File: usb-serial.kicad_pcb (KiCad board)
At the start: 4 copper layers, 68.5 x 42 mm, 42 parts, among them J2 DB25_Plug, U1 ACPL-M50L, U10 TDR2-1222WI, U11 PEME2-5-D12-D, U2 ACPL-M50L, U3 USBLC6-2SC6, U4 ACPL-M50L, U5 ACPL-M50L, U6 Interface_USB_CP2102N-A01-GQF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, U7 SN75155, U8 SN75155, U9 LM1117DT-5.0

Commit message: Add fabrication fies
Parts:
- F1: value Polyfuse -> Polyfuse 1,8A; footprint Fuse:Fuse_0805_2012Metric -> Fuse:Fuse_1206_3216Metric
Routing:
- net GND: track 20.1 -> 21.0 mm, vias 18 -> 20

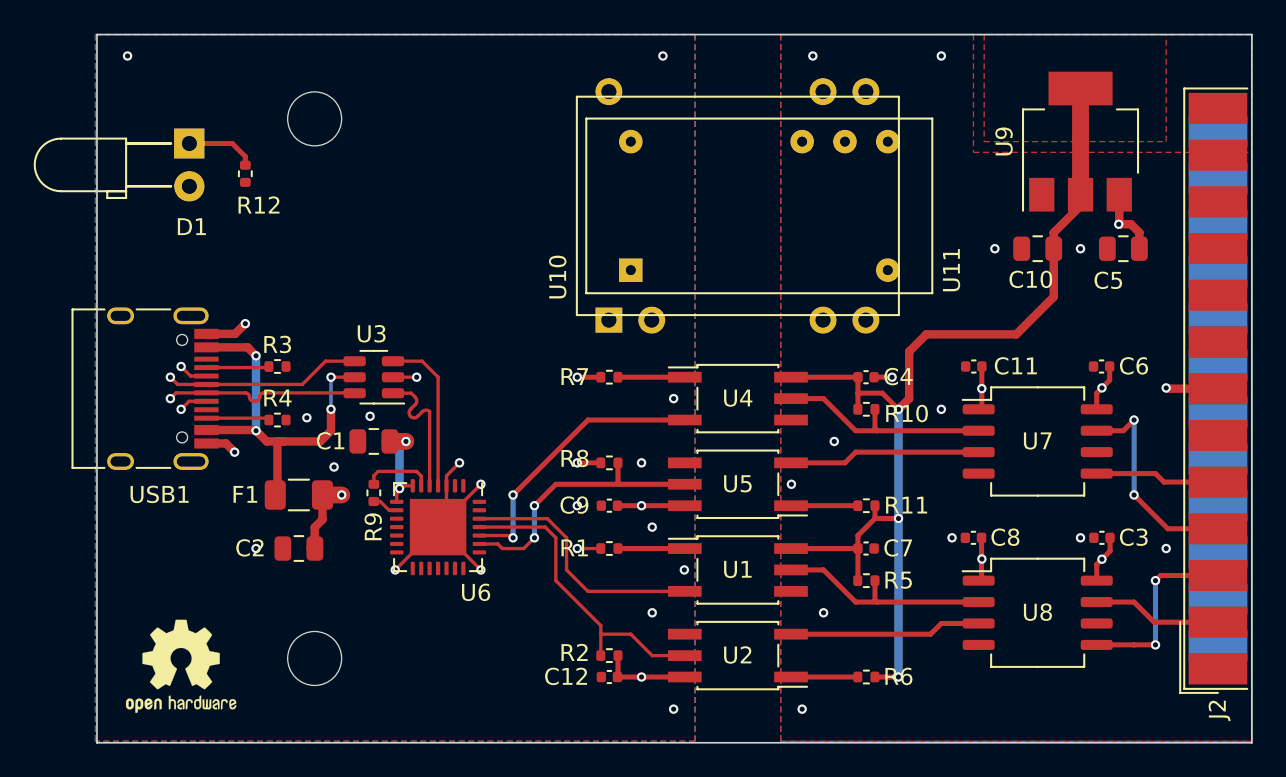
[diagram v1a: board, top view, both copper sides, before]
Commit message: EMC filter according to DC/DC datasheet
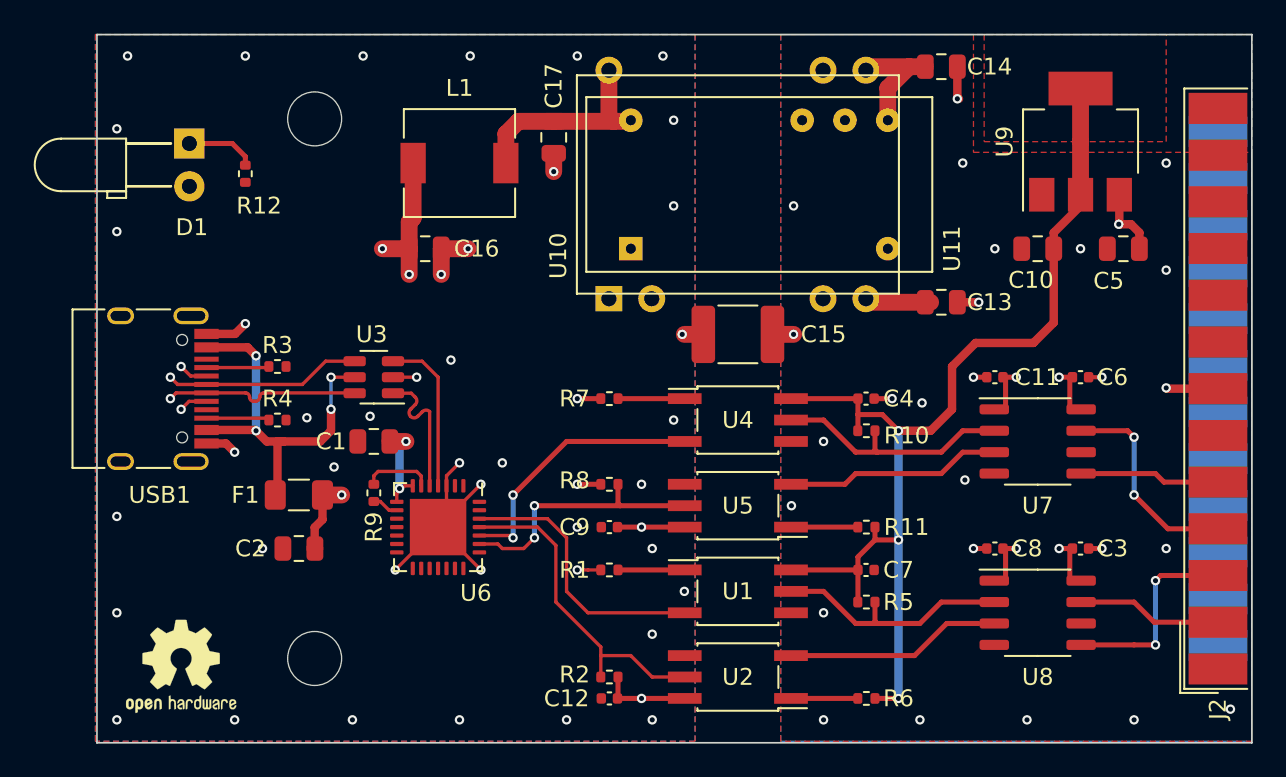
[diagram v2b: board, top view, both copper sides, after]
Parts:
- added C13: 1u, Capacitor_SMD:C_0805_2012Metric, F.Cu at (125.1, 48.9)
- added C14: 1u, Capacitor_SMD:C_0805_2012Metric, F.Cu at (125.1, 34.9)
- added C15: 220pF/3kV Y, Capacitor_SMD:C_1812_4532Metric, F.Cu at (113.0, 50.8)
- added C16: 10u, Capacitor_SMD:C_0805_2012Metric, F.Cu at (94.5, 45.7)
- added C17: 10u, Capacitor_SMD:C_0805_2012Metric, F.Cu at (102.1, 39.1)
- added L1: 2.2uH, Inductor_SMD:L_6.3x6.3_H3, F.Cu at (96.5, 40.6)
- U7, U8: footprint Package_SO:SO-8_5.3x6.2mm_P1.27mm -> Package_SO:SO-8_3.9x4.9mm_P1.27mm
- moved C3 1.42 mm to (133.3, 63.5), turned to 0 degrees
- moved C8 1.42 mm to (128.3, 63.5)
- moved C11 1.40 mm to (128.3, 53.3)
- moved C6 1.40 mm to (133.3, 53.3), turned to 0 degrees
- moved R2 1.27 mm to (105.4, 71.1)
- moved U1 1.27 mm to (113.0, 66.0)
- moved U2 1.27 mm to (113.0, 71.1)
- moved R10 1.27 mm to (120.7, 56.5)
- moved U11 1.27 mm to (106.7, 45.7)
- moved U4 1.27 mm to (113.0, 55.9)
- moved U5 1.27 mm to (113.0, 61.0)
- moved C12 1.27 mm to (105.4, 72.4)
- moved C4 1.27 mm to (120.6, 54.6)
- moved C7 1.27 mm to (120.6, 64.8)
- moved C9 1.27 mm to (105.4, 62.2)
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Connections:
- U10 pad 14: VBUS -> Vfilt
- U11 pad 14: VBUS -> Vfilt
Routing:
- net Vfilt: track 0.00 -> 12.6 mm
- net +12V: track 9.92 -> 18.4 mm
- net VBUS: track 23.6 -> 32.0 mm, vias 8 -> 10
- net GND1: track 4.15 -> 11.5 mm, vias 14 -> 26
- net -12V: track 5.25 -> 10.8 mm
- net GND: track 21.0 -> 26.3 mm, vias 20 -> 41
- net ~{ISO_CTS}: track 11.4 -> 12.8 mm
- net ~{ISO_TXD}: track 13.1 -> 14.6 mm
- net ~{ISO_RTS}: track 13.2 -> 14.7 mm
- net +5V: track 62.9 -> 64.1 mm
- net ~{TXD}: track 15.1 -> 16.4 mm
- net Net-(U7-DY): track 12.7 -> 11.6 mm
- net ~{RXD}: track 18.4 -> 19.4 mm
- net ~{ISO_RXD}: track 11.4 -> 11.9 mm
- net ~{RTS}: track 16.6 -> 16.1 mm
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
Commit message: usb-serial: Change opto to MAX 22246 isolator.
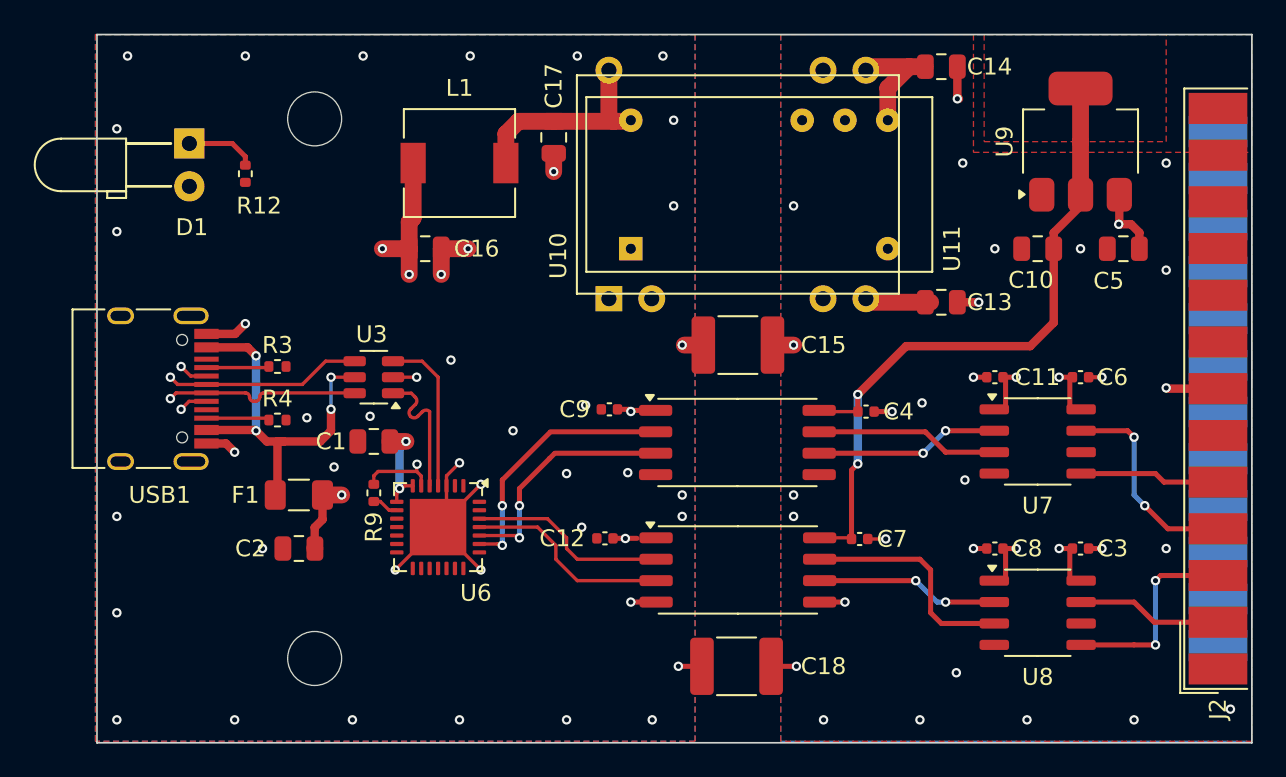
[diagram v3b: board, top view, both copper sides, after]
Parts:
- removed R1, R11, R6, R7: 1k, Resistor_SMD:R_0402_1005Metric
- removed R10, R2, R5, R8: 3k3, Resistor_SMD:R_0402_1005Metric
- removed REF**: OSHW-Logo2_7.3x6mm_SilkScreen, Symbol:OSHW-Logo2_7.3x6mm_SilkScreen
- removed U1, U2, U4, U5: ACPL-M50L, Package_SO:SO-5_4.4x3.6mm_P1.27mm
- added C18: 220pF/3kV Y, Capacitor_SMD:C_1812_4532Metric, F.Cu at (113.0, 70.5)
- added U12: MAX22246, anders:MAX22246, F.Cu at (113.0, 64.8)
- added U13: MAX22246, anders:MAX22246, F.Cu at (113.0, 57.2)
- R12: value 2k2 -> 1k5
- U11: value PEME2-5-D12-D -> <<<<<<s<
- moved C12 9.50 mm to (105.1, 62.9)
- moved C9 6.98 mm to (105.4, 55.2)
- moved C7 1.87 mm to (120.2, 62.9)
- moved C4 0.77 mm to (120.6, 55.4)
- moved C15 0.64 mm to (113.0, 51.4)
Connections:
- C12 pad 1: VBUS -> +3.3V
- C9 pad 1: VBUS -> +3.3V
- R9 pad 2: Net-(U6-VDD) -> +3.3V
- U6 pad 6: Net-(U6-VDD) -> +3.3V
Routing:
- net +3.3V: track 0.00 -> 28.5 mm, vias 0 -> 3
- net +5V: track 64.1 -> 42.3 mm, vias 3 -> 2
- net VBUS: track 32.0 -> 18.5 mm, vias 10 -> 5
- net ~{RXD}: track 19.4 -> 11.9 mm
- net ~{TXD}: track 16.4 -> 11.4 mm
- net Net-(U6-VDD): track 4.12 -> 0.00 mm
- net GND1: track 11.5 -> 15.5 mm, vias 26 -> 29
- net Net-(U5-A1): track 3.96 -> 0.00 mm
- net Net-(U4-A1): track 3.96 -> 0.00 mm
- net Net-(U2-A1): track 3.96 -> 0.00 mm
- net Net-(U1-A1): track 3.96 -> 0.00 mm
- net ~{ISO_RTS}: track 14.7 -> 10.9 mm, vias 0 -> 2
- net ~{ISO_TXD}: track 14.6 -> 11.4 mm, vias 0 -> 2
- net GND: track 26.3 -> 29.2 mm, vias 41 -> 43
- net ~{ISO_RXD}: track 11.9 -> 13.9 mm
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- added copper zone on In2.Cu, net GND
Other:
- board text added: "Isolated USB-RS232 Adapter By Anders Sandahl 2024/2025"
- board text removed: "Isolated USB-RS232 Adapter By Anders Sandahl 2024"

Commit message: Updated 3D image of PCB
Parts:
- U11: value <<<<<<s< -> PEME2-5-D12-D
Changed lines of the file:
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@@
 			)
 		)
-		(property "Value" "<<<<<<s<"
+		(property "Value" "PEME2-5-D12-D"
 			(at 7.43 20.32 90)
 			(layer "F.Fab")
@@
 		(sheetname "Root")
 		(sheetfile "usb-serial.kicad_sch")
-		(attr through_hole exclude_from_pos_files exclude_from_bom)
+		(attr through_hole exclude_from_pos_files)
 		(fp_line
 			(start 8.99 -2.64)
@@
 		)
 		(property "Footprint" "LED_THT:LED_D3.0mm_Horizontal_O3.81mm_Z10.0mm"
-			(at 0 0 -90)
+			(at 0 0 90)
 			(layer "F.Fab")
 			(hide yes)
@@
 		)
 		(property "Datasheet" ""
-			(at 0 0 -90)
+			(at 0 0 90)
 			(layer "F.Fab")
 			(hide yes)
@@
 		)
 		(property "Description" ""
-			(at 0 0 -90)
+			(at 0 0 90)
 			(layer "F.Fab")
 			(hide yes)
@@
 		(sheetname "Root")
 		(sheetfile "usb-serial.kicad_sch")
-		(attr through_hole exclude_from_pos_files exclude_from_bom)
+		(attr through_hole exclude_from_pos_files)
 		(fp_line
 			(start 2.83 4.87)
@@
 		)
 		(fp_text user "${REFERENCE}"
-			(at 1.27 5.66 -90)
+			(at 1.27 5.66 90)
 			(layer "F.Fab")
 			(effects
@@
 		(model "${KICAD8_3DMODEL_DIR}/LED_THT.3dshapes/LED_D3.0mm_Horizontal_O3.81mm_Z10.0mm.wrl"
 			(offset
-				(xyz 0 0 0)
+				(xyz 0 0 -8)
 			)
 			(scale
@@
 		(sheetname "Root")
 		(sheetfile "usb-serial.kicad_sch")
-		(attr exclude_from_pos_files exclude_from_bom)
+		(attr exclude_from_pos_files)
 		(fp_circle
 			(center 0 0)
@@
 		(sheetname "Root")
 		(sheetfile "usb-serial.kicad_sch")
-		(attr smd exclude_from_pos_files exclude_from_bom)
+		(attr smd exclude_from_pos_files)
 		(fp_line
 			(start -18.043333 -2.24)
@@
 			(pintype "passive+no_connect")
 		)
-		(model "${KICAD8_3DMODEL_DIR}/Connector_Dsub.3dshapes/DSUB-25_Male_EdgeMount_P2.77mm.wrl"
+		(model "/home/anders/.local/share/kicad/8.0/3dmodels/dsub-db25-male-171-025-103.STEP"
 			(offset
-				(xyz 0 0 0)
+				(xyz -26.5 -8.5 -6.9)
 			)
 			(scale
@@
 			)
 			(rotate
-				(xyz 0 0 0)
+				(xyz 90 180 180)
 			)
 		)
@@
 		(sheetname "Root")
 		(sheetfile "usb-serial.kicad_sch")
-		(attr through_hole exclude_from_pos_files exclude_from_bom)
+		(attr through_hole exclude_from_pos_files)
 		(fp_line
 			(start 13.25 -1.9)
@@
 		(sheetname "Root")
 		(sheetfile "usb-serial.kicad_sch")
-		(attr exclude_from_pos_files exclude_from_bom)
+		(attr exclude_from_pos_files)
 		(fp_circle
 			(center 0 0)

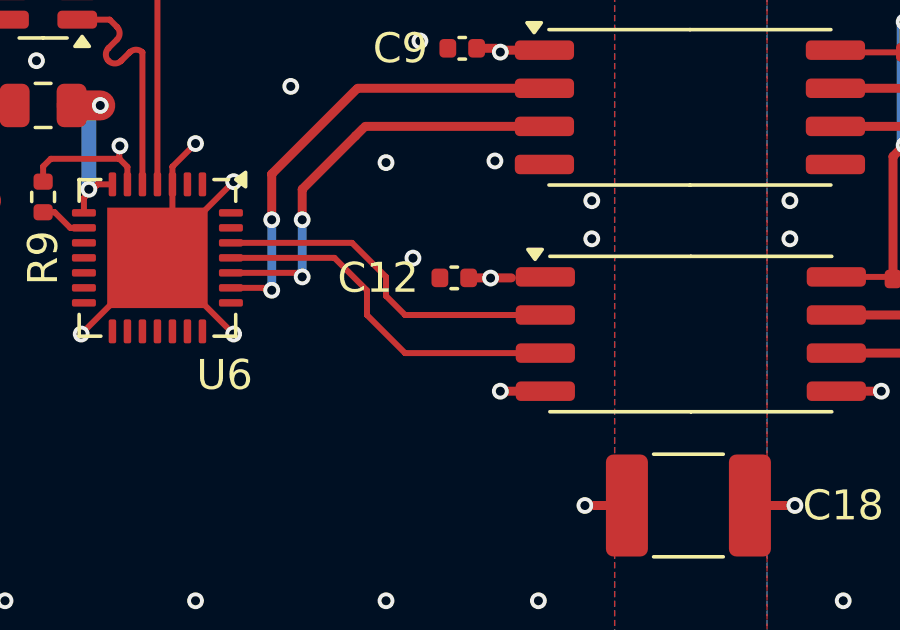
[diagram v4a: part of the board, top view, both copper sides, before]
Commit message: usb-serial: Fix swapped RXD and TXD
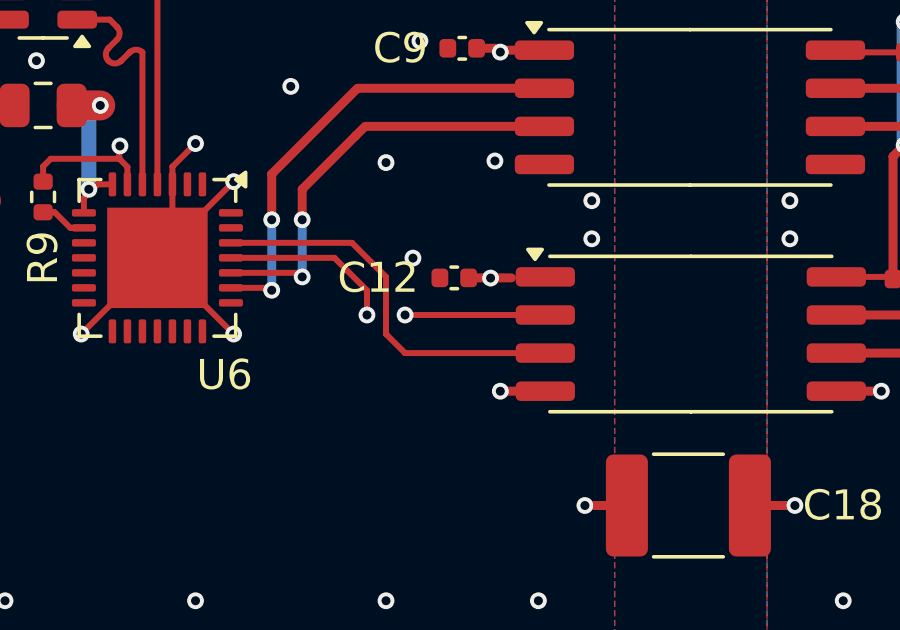
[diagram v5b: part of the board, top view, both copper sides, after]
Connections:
- U12 pad 2: ~{TXD} -> ~{RXD}
- U12 pad 3: ~{RXD} -> ~{TXD}
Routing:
- net ~{TXD}: track 11.4 -> 8.44 mm
- net ~{RXD}: track 11.9 -> 11.3 mm, vias 0 -> 2
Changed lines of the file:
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@@
 			(layers "F.Cu" "F.Paste" "F.Mask")
 			(roundrect_rratio 0.25)
-			(net 38 "~{TXD}")
+			(net 34 "~{RXD}")
 			(pinfunction "OUT1")
 			(pintype "output")
@@
 			(layers "F.Cu" "F.Paste" "F.Mask")
 			(roundrect_rratio 0.25)
-			(net 34 "~{RXD}")
+			(net 38 "~{TXD}")
 			(pinfunction "IN2")
 			(pintype "input")
@@
 		)
 	)
+	(gr_line
+		(start 107.95 65.405)
+		(end 103.505 65.405)
+		(stroke
+			(width 0.2)
+			(type default)
+		)
+		(layer "F.Cu")
+		(net 38)
+	)
 	(gr_rect
 		(start 75.02 33.02)
@@
 	)
 	(segment
-		(start 103.505 65.405)
-		(end 102.235 64.135)
-		(width 0.2)
-		(layer "F.Cu")
-		(net 34)
-	)
-	(segment
-		(start 107.775 65.405)
-		(end 103.505 65.405)
+		(start 101.150244 62.23)
+		(end 97.7 62.23)
 		(width 0.2)
 		(layer "F.Cu")
@@
 	)
 	(segment
-		(start 101.150244 62.23)
-		(end 97.7 62.23)
+		(start 107.775 64.135)
+		(end 103.505 64.135)
 		(width 0.2)
 		(layer "F.Cu")
@@
 		(net 34)
 	)
+	(via
+		(at 103.505 64.135)
+		(size 0.56)
+		(drill 0.3)
+		(layers "F.Cu" "B.Cu")
+		(net 34)
+	)
+	(via
+		(at 102.235 64.135)
+		(size 0.56)
+		(drill 0.3)
+		(layers "F.Cu" "B.Cu")
+		(net 34)
+	)
+	(segment
+		(start 102.235 64.135)
+		(end 103.505 64.135)
+		(width 0.25)
+		(layer "In2.Cu")
+		(net 34)
+	)
 	(segment
 		(start 117.475 65.405)
@@
 	)
 	(segment
-		(start 107.775 64.135)
-		(end 103.505 64.135)
+		(start 103.505 65.405)
+		(end 102.87 64.77)
 		(width 0.2)
 		(layer "F.Cu")
@@
 	)
 	(segment
-		(start 102.87 62.865)
-		(end 101.735 61.73)
+		(start 102.87 64.77)
+		(end 102.87 62.865)
 		(width 0.2)
 		(layer "F.Cu")
@@
 	)
 	(segment
-		(start 103.505 64.135)
-		(end 102.87 63.5)
+		(start 102.87 62.865)
+		(end 101.735 61.73)
 		(width 0.2)
 		(layer "F.Cu")
@@
 		(width 0.2)
 		(layer "F.Cu")
-		(net 38)
-	)
-	(segment
-		(start 102.87 63.5)
-		(end 102.87 62.865)
-		(width 0.2)
-		(layer "F.Cu")
